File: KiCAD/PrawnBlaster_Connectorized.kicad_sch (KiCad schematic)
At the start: 30 parts, among them IC1 74LVT245D,118, J1 Int. Clock, J2 Ext. Clock, J3 Ext. Trig., J4 Pseudoclock 3, J5 Pseudoclock 1, J6 Pseudoclock 2, J7 Pseudoclock 0, U1 74LVC1G34, U2 74LVC1G34, U3 Pico, U4 74LVC1G17

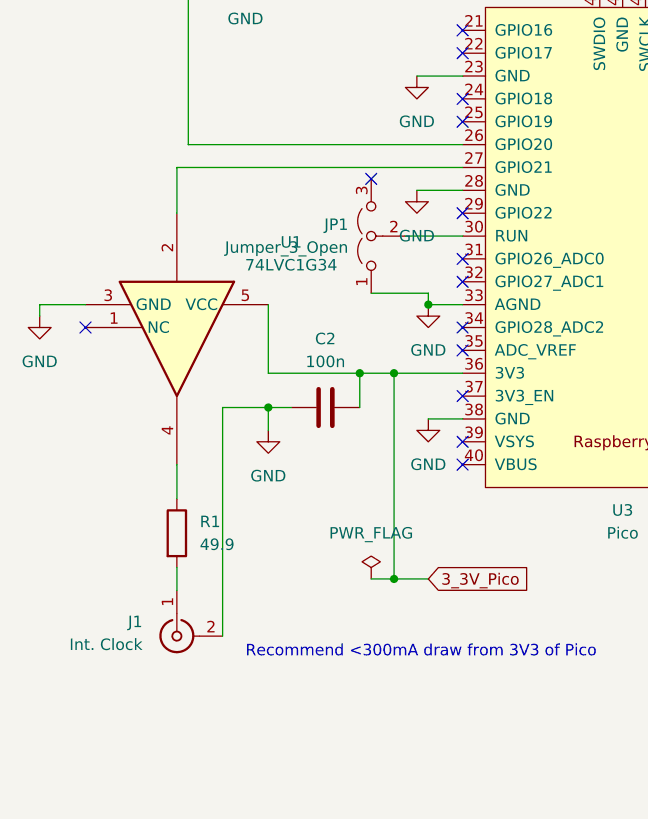
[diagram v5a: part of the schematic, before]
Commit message: Remove internal clock output (that doesn't currently exist).
Update LOGO to be slightly larger and cropped. Add another mount hole.
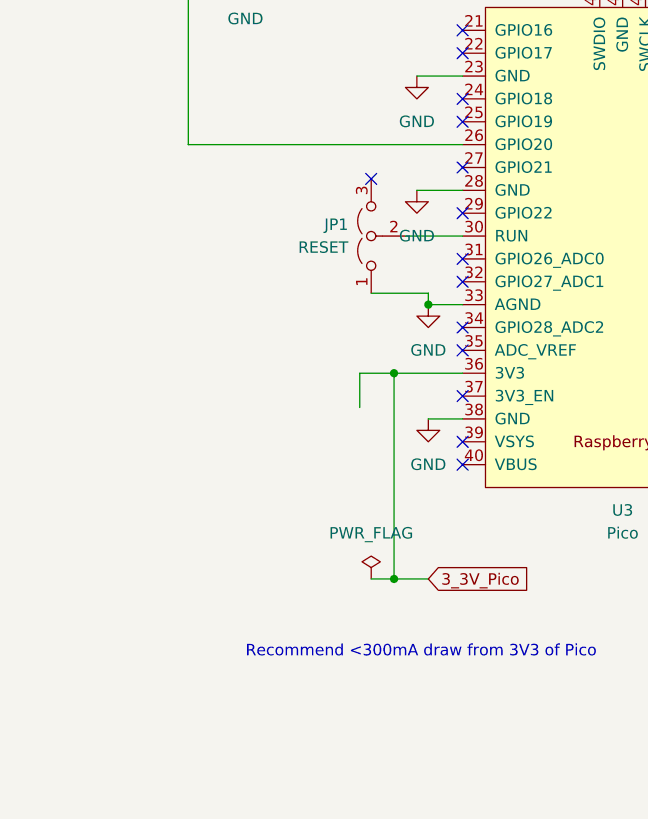
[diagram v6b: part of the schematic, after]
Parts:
- removed C2: 100n, Capacitor_SMD:C_0805_2012Metric_Pad1.18x1.45mm_HandSolder, symbol Device:C
- removed J1: Int. Clock, Connector_Coaxial:SMA_Amphenol_132289_EdgeMount, symbol Connector:Conn_Coaxial
- removed R1: 49.9, Resistor_SMD:R_1206_3216Metric_Pad1.30x1.75mm_HandSolder, symbol Device:R
- removed U1: 74LVC1G34, Package_TO_SOT_SMD:SOT-23-5_HandSoldering, symbol 74xGxx:74LVC1G34
- JP1: value Jumper_3_Open -> RESET
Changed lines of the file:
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@@
   (junction (at 162.56 129.54) (diameter 0) (color 0 0 0 0)
   )
-  (junction (at 44.45 113.03) (diameter 0) (color 0 0 0 0)
-  )
   (junction (at 171.45 82.55) (diameter 0) (color 0 0 0 0)
   )
@@
   )
   (junction (at 171.45 66.04) (diameter 0) (color 0 0 0 0)
-  )
-  (junction (at 54.61 109.22) (diameter 0) (color 0 0 0 0)
   )
   (junction (at 146.05 82.55) (diameter 0) (color 0 0 0 0)
@@
   (no_connect (at 101.6 109.22))
   (no_connect (at 101.6 111.76))
-  (no_connect (at 24.13 104.14))
+  (no_connect (at 66.04 86.36))
   (no_connect (at 66.04 81.28))
   (no_connect (at 66.04 78.74))
@@
     (stroke (width 0) (type default))
   )
-  (wire (pts (xy 44.45 113.03) (xy 44.45 115.57))
-    (stroke (width 0) (type default))
-  )
   (wire (pts (xy 74.93 48.26) (xy 74.93 46.99))
     (stroke (width 0) (type default))
@@
     (stroke (width 0) (type default))
   )
-  (wire (pts (xy 24.13 101.6) (xy 19.05 101.6))
-    (stroke (width 0) (type default))
-  )
   (wire (pts (xy 55.88 132.08) (xy 58.42 132.08))
     (stroke (width 0) (type default))
@@
     (stroke (width 0) (type default))
   )
-  (wire (pts (xy 44.45 109.22) (xy 54.61 109.22))
-    (stroke (width 0) (type default))
-  )
   (wire (pts (xy 58.42 132.08) (xy 62.23 132.08))
     (stroke (width 0) (type default))
@@
     (stroke (width 0) (type default))
   )
-  (wire (pts (xy 34.29 130.81) (xy 34.29 133.35))
-    (stroke (width 0) (type default))
-  )
-  (wire (pts (xy 44.45 113.03) (xy 46.99 113.03))
-    (stroke (width 0) (type default))
-  )
   (wire (pts (xy 210.82 62.23) (xy 210.82 69.85))
     (stroke (width 0) (type default))
@@
     (stroke (width 0) (type default))
   )
-  (wire (pts (xy 34.29 119.38) (xy 34.29 123.19))
-    (stroke (width 0) (type default))
-  )
   (wire (pts (xy 193.04 82.55) (xy 224.79 82.55))
     (stroke (width 0) (type default))
@@
     (stroke (width 0) (type default))
   )
-  (wire (pts (xy 19.05 101.6) (xy 19.05 102.87))
-    (stroke (width 0) (type default))
-  )
   (wire (pts (xy 52.07 62.23) (xy 53.34 62.23))
     (stroke (width 0) (type default))
@@
     (stroke (width 0) (type default))
   )
-  (wire (pts (xy 66.04 86.36) (xy 34.29 86.36))
-    (stroke (width 0) (type default))
-  )
   (wire (pts (xy 269.24 22.86) (xy 269.24 25.4))
     (stroke (width 0) (type default))
@@
     (stroke (width 0) (type default))
   )
-  (wire (pts (xy 39.37 113.03) (xy 44.45 113.03))
-    (stroke (width 0) (type default))
-  )
   (wire (pts (xy 133.35 119.38) (xy 138.43 119.38))
     (stroke (width 0) (type default))
   )
-  (wire (pts (xy 44.45 101.6) (xy 44.45 109.22))
-    (stroke (width 0) (type default))
-  )
   (wire (pts (xy 137.16 74.93) (xy 146.05 74.93))
     (stroke (width 0) (type default))
@@
     (stroke (width 0) (type default))
   )
-  (wire (pts (xy 34.29 86.36) (xy 34.29 91.44))
-    (stroke (width 0) (type default))
-  )
   (wire (pts (xy 193.04 92.71) (xy 224.79 92.71))
-    (stroke (width 0) (type default))
-  )
-  (wire (pts (xy 39.37 113.03) (xy 39.37 138.43))
     (stroke (width 0) (type default))
   )
@@
     )
   )
-  (symbol (lib_id "Connector:Conn_Coaxial") (at 34.29 138.43 90) (mirror x) (unit 1)
-    (in_bom yes) (on_board yes) (dnp no) (fields_autoplaced)
-    (property "Reference" "J1" (at 30.48 136.8425 90)
-      (effects (font (size 1.27 1.27)) (justify left))
-    )
-    (property "Value" "Int. Clock" (at 30.48 139.3825 90)
-      (effects (font (size 1.27 1.27)) (justify left))
-    )
-    (property "Footprint" "Connector_Coaxial:SMA_Amphenol_132289_EdgeMount" (at 34.29 138.43 0)
-      (effects (font (size 1.27 1.27)) hide)
-    )
-    (property "Datasheet" " ~" (at 34.29 138.43 0)
-      (effects (font (size 1.27 1.27)) hide)
-    )
-    (pin "1")
-    (pin "2")
-    (instances
-      (project "PrawnBlaster_Connectorized"
-        (path "/aa2b0f9c-998a-4cca-8380-404df994482a"
-          (reference "J1") (unit 1)
-        )
-      )
-    )
-  )
   (symbol (lib_id "Device:R") (at 113.03 96.52 180) (unit 1)
     (in_bom yes) (on_board yes) (dnp no)
@@
         (path "/aa2b0f9c-998a-4cca-8380-404df994482a"
           (reference "#PWR06") (unit 1)
-        )
-      )
-    )
-  )
-  (symbol (lib_id "power:GND") (at 44.45 115.57 0) (unit 1)
-    (in_bom yes) (on_board yes) (dnp no)
-    (property "Reference" "#PWR03" (at 44.45 121.92 0)
-      (effects (font (size 1.27 1.27)) hide)
-    )
-    (property "Value" "GND" (at 44.45 120.65 0)
-      (effects (font (size 1.27 1.27)))
-    )
-    (property "Footprint" "" (at 44.45 115.57 0)
-      (effects (font (size 1.27 1.27)) hide)
-    )
-    (property "Datasheet" "" (at 44.45 115.57 0)
-      (effects (font (size 1.27 1.27)) hide)
-    )
-    (pin "1")
-    (instances
-      (project "PrawnBlaster_Connectorized"
-        (path "/aa2b0f9c-998a-4cca-8380-404df994482a"
-          (reference "#PWR03") (unit 1)
-        )
-      )
-    )
-  )
-  (symbol (lib_id "power:GND") (at 19.05 102.87 0) (unit 1)
-    (in_bom yes) (on_board yes) (dnp no)
-    (property "Reference" "#PWR01" (at 19.05 109.22 0)
-      (effects (font (size 1.27 1.27)) hide)
-    )
-    (property "Value" "GND" (at 19.05 107.95 0)
-      (effects (font (size 1.27 1.27)))
-    )
-    (property "Footprint" "" (at 19.05 102.87 0)
-      (effects (font (size 1.27 1.27)) hide)
-    )
-    (property "Datasheet" "" (at 19.05 102.87 0)
-      (effects (font (size 1.27 1.27)) hide)
-    )
-    (pin "1")
-    (instances
-      (project "PrawnBlaster_Connectorized"
-        (path "/aa2b0f9c-998a-4cca-8380-404df994482a"
-          (reference "#PWR01") (unit 1)
         )
       )
@@
       (effects (font (size 1.27 1.27)) (justify left))
     )
-    (property "Value" "Jumper_3_Open" (at 53.34 95.25 90)
+    (property "Value" "RESET" (at 53.34 95.25 90)
       (effects (font (size 1.27 1.27)) (justify left))
     )
@@
     )
   )
-  (symbol (lib_id "Device:C") (at 50.8 113.03 270) (unit 1)
-    (in_bom yes) (on_board yes) (dnp no) (fields_autoplaced)
-    (property "Reference" "C2" (at 50.8 105.41 90)
-      (effects (font (size 1.27 1.27)))
-    )
-    (property "Value" "100n" (at 50.8 107.95 90)
-      (effects (font (size 1.27 1.27)))
-    )
-    (property "Footprint" "Capacitor_SMD:C_0805_2012Metric_Pad1.18x1.45mm_HandSolder" (at 46.99 113.9952 0)
-      (effects (font (size 1.27 1.27)) hide)
-    )
-    (property "Datasheet" "~" (at 50.8 113.03 0)
-      (effects (font (size 1.27 1.27)) hide)
-    )
-    (pin "1")
-    (pin "2")
-    (instances
-      (project "PrawnBlaster_Connectorized"
-        (path "/aa2b0f9c-998a-4cca-8380-404df994482a"
-          (reference "C2") (unit 1)
-        )
-      )
-    )
-  )
   (symbol (lib_id "Device:R") (at 162.56 137.16 180) (unit 1)
     (in_bom yes) (on_board yes) (dnp no) (fields_autoplaced)
@@
     )
   )
-  (symbol (lib_id "Device:R") (at 34.29 127 0) (unit 1)
-    (in_bom yes) (on_board yes) (dnp no) (fields_autoplaced)
-    (property "Reference" "R1" (at 36.83 125.73 0)
-      (effects (font (size 1.27 1.27)) (justify left))
-    )
-    (property "Value" "49.9" (at 36.83 128.27 0)
-      (effects (font (size 1.27 1.27)) (justify left))
-    )
-    (property "Footprint" "Resistor_SMD:R_1206_3216Metric_Pad1.30x1.75mm_HandSolder" (at 32.512 127 90)
-      (effects (font (size 1.27 1.27)) hide)
-    )
-    (property "Datasheet" "~" (at 34.29 127 0)
-      (effects (font (size 1.27 1.27)) hide)
-    )
-    (pin "1")
-    (pin "2")
-    (instances
-      (project "PrawnBlaster_Connectorized"
-        (path "/aa2b0f9c-998a-4cca-8380-404df994482a"
-          (reference "R1") (unit 1)
-        )
-      )
-    )
-  )
   (symbol (lib_id "power:GND") (at 138.43 142.24 0) (unit 1)
     (in_bom yes) (on_board yes) (dnp no) (fields_autoplaced)
@@
         )
       )
-    )
-  )
-  (symbol (lib_id "74xGxx:74LVC1G34") (at 34.29 106.68 270) (unit 1)
-    (in_bom yes) (on_board yes) (dnp no) (fields_autoplaced)
-    (property "Reference" "U1" (at 46.99 94.6719 90)
-      (effects (font (size 1.27 1.27)))
-    )
-    (property "Value" "74LVC1G34" (at 46.99 97.2119 90)
-      (effects (font (size 1.27 1.27)))
-    )
-    (property "Footprint" "Package_TO_SOT_SMD:SOT-23-5_HandSoldering" (at 34.29 106.68 0)
-      (effects (font (size 1.27 1.27)) hide)
-    )
-    (property "Datasheet" "https://www.ti.com/lit/ds/symlink/sn74lvc1g34.pdf" (at 34.29 106.68 0)
-      (effects (font (size 1.27 1.27)) hide)
-    )
-    (pin "1")
-    (pin "2")
-    (pin "3")
-    (pin "4")
-    (pin "5")
-    (instances
-      (project "PrawnBlaster_Connectorized"
-        (path "/aa2b0f9c-998a-4cca-8380-404df994482a"
-          (reference "U1") (unit 1)
-        )
-      )

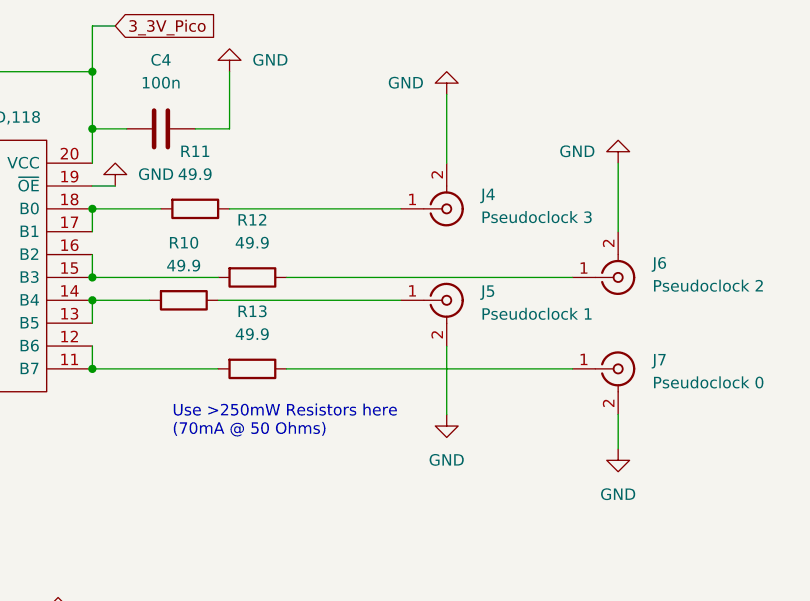
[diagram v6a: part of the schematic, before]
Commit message: Minor tweaks to help have more accurate 50ohm transmission lines on the outputs.
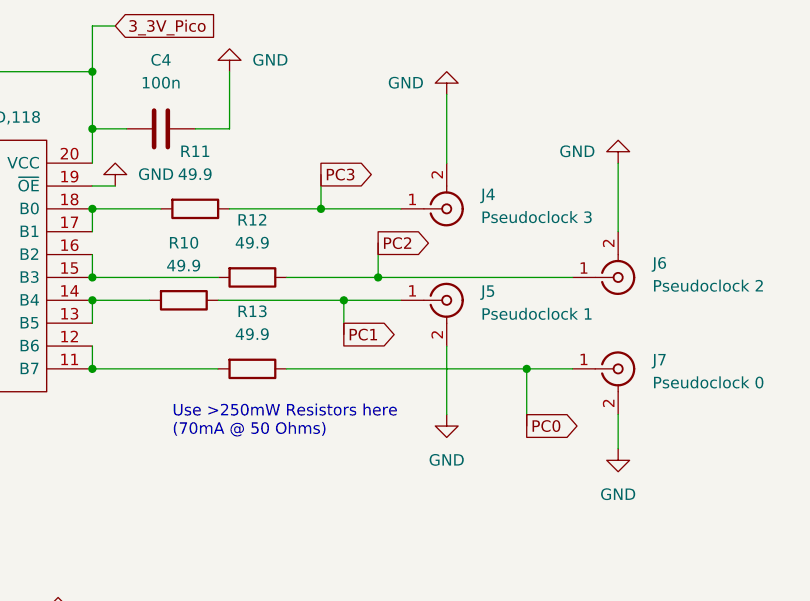
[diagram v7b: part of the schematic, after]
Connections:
- net PC3: now reaches J4.1 (In), R11.1
- net PC1: now reaches J5.1 (In), R10.1
- net PC0: now reaches J7.1 (In), R13.1
- net PC2: now reaches J6.1 (In), R12.1
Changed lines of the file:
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@@
   (junction (at 171.45 74.93) (diameter 0) (color 0 0 0 0)
   )
+  (junction (at 199.39 85.09) (diameter 0) (color 0 0 0 0)
+  )
   (junction (at 171.45 92.71) (diameter 0) (color 0 0 0 0)
   )
@@
   (junction (at 171.45 66.04) (diameter 0) (color 0 0 0 0)
   )
+  (junction (at 219.71 92.71) (diameter 0) (color 0 0 0 0)
+  )
   (junction (at 146.05 82.55) (diameter 0) (color 0 0 0 0)
   )
+  (junction (at 196.85 74.93) (diameter 0) (color 0 0 0 0)
+  )
   (junction (at 58.42 109.22) (diameter 0) (color 0 0 0 0)
   )
@@
   )
   (junction (at 123.19 78.74) (diameter 0) (color 0 0 0 0)
+  )
+  (junction (at 203.2 82.55) (diameter 0) (color 0 0 0 0)
   )
   (junction (at 62.23 101.6) (diameter 0) (color 0 0 0 0)
@@
     (stroke (width 0) (type default))
   )
-  (wire (pts (xy 186.69 74.93) (xy 205.74 74.93))
+  (wire (pts (xy 186.69 74.93) (xy 196.85 74.93))
+    (stroke (width 0) (type default))
+  )
+  (wire (pts (xy 199.39 85.09) (xy 205.74 85.09))
     (stroke (width 0) (type default))
   )
@@
     (stroke (width 0) (type default))
   )
-  (wire (pts (xy 185.42 85.09) (xy 205.74 85.09))
+  (wire (pts (xy 185.42 85.09) (xy 199.39 85.09))
     (stroke (width 0) (type default))
   )
@@
     (stroke (width 0) (type default))
   )
+  (wire (pts (xy 199.39 85.09) (xy 199.39 88.9))
+    (stroke (width 0) (type default))
+  )
   (wire (pts (xy 167.64 120.65) (xy 167.64 124.46))
     (stroke (width 0) (type default))
@@
     (stroke (width 0) (type default))
   )
+  (wire (pts (xy 196.85 71.12) (xy 196.85 74.93))
+    (stroke (width 0) (type default))
+  )
   (wire (pts (xy 210.82 62.23) (xy 210.82 69.85))
     (stroke (width 0) (type default))
   )
+  (wire (pts (xy 219.71 92.71) (xy 219.71 99.06))
+    (stroke (width 0) (type default))
+  )
   (wire (pts (xy 62.23 114.3) (xy 66.04 114.3))
     (stroke (width 0) (type default))
@@
     (stroke (width 0) (type default))
   )
-  (wire (pts (xy 193.04 82.55) (xy 224.79 82.55))
+  (wire (pts (xy 203.2 82.55) (xy 224.79 82.55))
+    (stroke (width 0) (type default))
+  )
+  (wire (pts (xy 193.04 82.55) (xy 203.2 82.55))
     (stroke (width 0) (type default))
   )
@@
     (stroke (width 0) (type default))
   )
+  (wire (pts (xy 219.71 92.71) (xy 224.79 92.71))
+    (stroke (width 0) (type default))
+  )
   (wire (pts (xy 229.87 69.85) (xy 229.87 77.47))
     (stroke (width 0) (type default))
@@
     (stroke (width 0) (type default))
   )
+  (wire (pts (xy 196.85 74.93) (xy 205.74 74.93))
+    (stroke (width 0) (type default))
+  )
   (wire (pts (xy 62.23 100.33) (xy 62.23 101.6))
     (stroke (width 0) (type default))
@@
     (stroke (width 0) (type default))
   )
+  (wire (pts (xy 203.2 78.74) (xy 203.2 82.55))
+    (stroke (width 0) (type default))
+  )
   (wire (pts (xy 133.35 110.49) (xy 135.89 110.49))
     (stroke (width 0) (type default))
   )
-  (wire (pts (xy 193.04 92.71) (xy 224.79 92.71))
+  (wire (pts (xy 193.04 92.71) (xy 219.71 92.71))
     (stroke (width 0) (type default))
   )
@@
     )
   )
+  (global_label "PC2" (shape output) (at 203.2 78.74 0) (fields_autoplaced)
+    (effects (font (size 1.27 1.27)) (justify left))
+    (property "Intersheetrefs" "${INTERSHEET_REFS}" (at 209.9347 78.74 0)
+      (effects (font (size 1.27 1.27)) (justify left) hide)
+    )
+  )
+  (global_label "PC3" (shape output) (at 196.85 71.12 0) (fields_autoplaced)
+    (effects (font (size 1.27 1.27)) (justify left))
+    (property "Intersheetrefs" "${INTERSHEET_REFS}" (at 203.5847 71.12 0)
+      (effects (font (size 1.27 1.27)) (justify left) hide)
+    )
+  )
   (global_label "3_3V_Pico" (shape input) (at 58.42 62.23 0) (fields_autoplaced)
     (effects (font (size 1.27 1.27)) (justify left))
@@
     )
   )
+  (global_label "PC1" (shape output) (at 199.39 88.9 0) (fields_autoplaced)
+    (effects (font (size 1.27 1.27)) (justify left))
+    (property "Intersheetrefs" "${INTERSHEET_REFS}" (at 206.1247 88.9 0)
+      (effects (font (size 1.27 1.27)) (justify left) hide)
+    )
+  )
   (global_label "3_3V_Pico" (shape input) (at 173.99 54.61 0) (fields_autoplaced)
     (effects (font (size 1.27 1.27)) (justify left))
@@
       (effects (font (size 1.27 1.27)) (justify left) hide)
     )
+  )
+  (global_label "PC0" (shape output) (at 219.71 99.06 0) (fields_autoplaced)
+    (effects (font (size 1.27 1.27)) (justify left))
+    (property "Intersheetrefs" "${INTERSHEET_REFS}" (at 226.4447 99.06 0)
+      (effects (font (size 1.27 1.27)) (justify left) hide)
+    )
